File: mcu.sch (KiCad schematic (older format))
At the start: 23 parts, among them U6 LPC55S16JBD64E, Y1 16 MHz, Y2 32.768 kHz

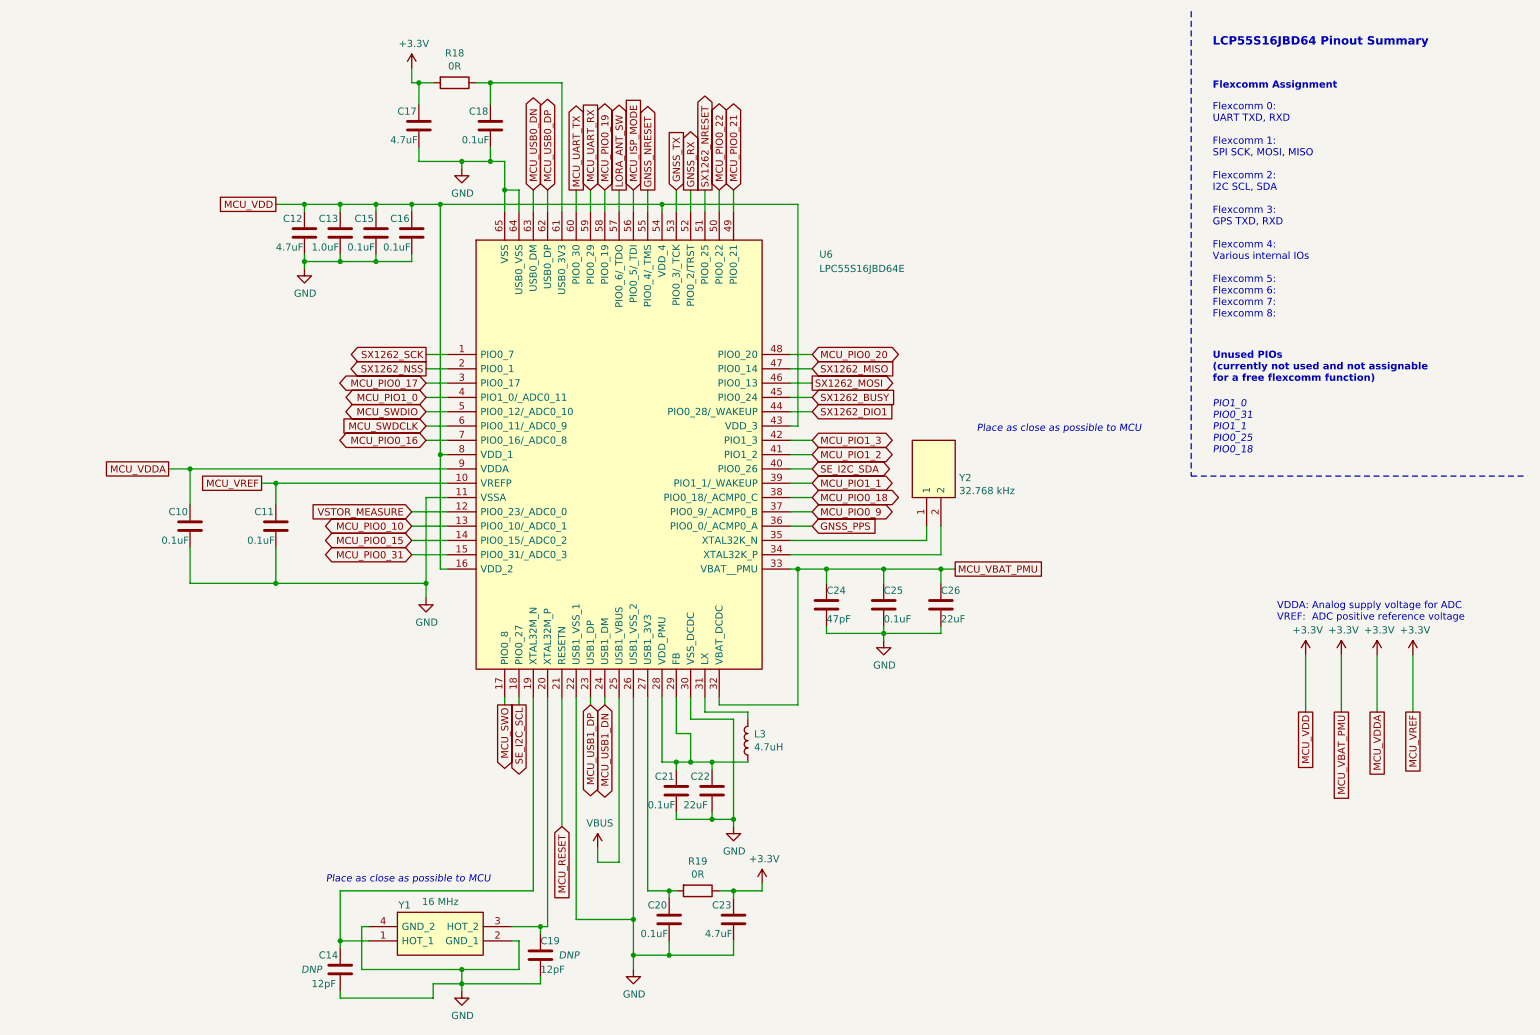
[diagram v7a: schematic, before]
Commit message: Changed pin assignment on mcu and extension header
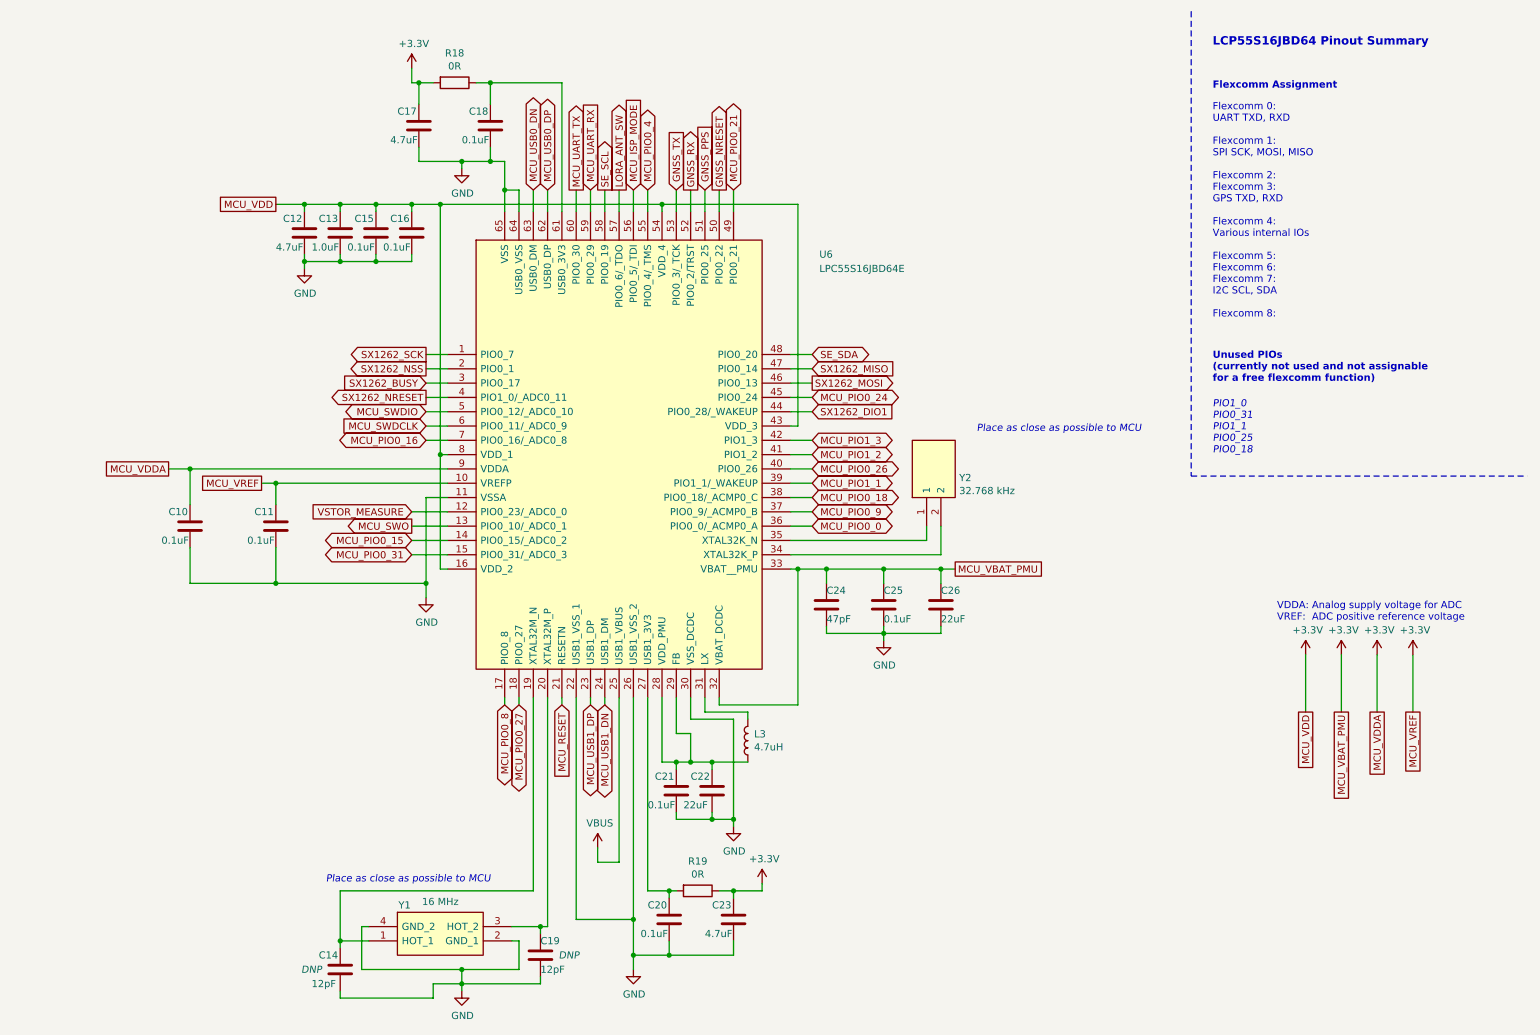
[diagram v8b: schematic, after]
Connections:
- net MCU_PIO0_10 is gone; now on net MCU_SWO: U6.13 (PIO0_10/_ADC0_1)
- net MCU_PIO0_17 is gone; now on net SX1262_BUSY: U6.3 (PIO0_17)
- net MCU_PIO0_22 is gone; now on net GNSS_NRESET: U6.50 (PIO0_22)
- net MCU_PIO1_0 is gone; now on net SX1262_NRESET: U6.4 (PIO1_0/_ADC0_11)
- net GNSS_NRESET: no longer U6.55 (PIO0_4/_TMS)
- net GNSS_PPS: now also U6.51 (PIO0_25); no longer U6.36 (PIO0_0/_ACMP0_A)
- net MCU_SWO: no longer U6.17 (PIO0_8)
- net SX1262_BUSY: no longer U6.45 (PIO0_24)
- net SX1262_NRESET: no longer U6.51 (PIO0_25)
- net MCU_PIO0_19 renamed SE_SCL
- net MCU_PIO0_20 renamed SE_SDA
- net SE_I2C_SCL renamed MCU_PIO0_27
- net SE_I2C_SDA renamed MCU_PIO0_26
- new net MCU_PIO0_0: U6.36 (PIO0_0/_ACMP0_A)
- new net MCU_PIO0_24: U6.45 (PIO0_24)
- new net MCU_PIO0_4: U6.55 (PIO0_4/_TMS)
- new net MCU_PIO0_8: U6.17 (PIO0_8)
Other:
- note added: "Flexcomm 0:\nUART TXD, RXD\n\nFlexcomm 1:\nSPI SCK, MOSI, MISO\n\nFlexcomm 2:\nFlexcomm 3:\nGPS TXD, RXD\n\nFlexcomm 4:\nVarious internal IOs\n\nFlexcomm 5:\nFlexcomm 6:\nFlexcomm 7:\nI2C SCL, SDA\n\nFlexcomm 8:"
- note removed: "Flexcomm 0:\nUART TXD, RXD\n\nFlexcomm 1:\nSPI SCK, MOSI, MISO\n\nFlexcomm 2:\nI2C SCL, SDA\n\nFlexcomm 3:\nGPS TXD, RXD\n\nFlexcomm 4:\nVarious internal IOs\n\nFlexcomm 5:\nFlexcomm 6:\nFlexcomm 7:\nFlexcomm 8:"
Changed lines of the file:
@@
 Wire Wire Line
 	3500 7300 3700 7300
-Text GLabel 4400 6200 3    50   Input ~ 0
+Text GLabel 4400 5350 3    50   Input ~ 0
 MCU_RESET
 Wire Wire Line
-	4400 5300 4400 6200
+	4400 5300 4400 5350
 Text GLabel 4700 5350 3    50   BiDi ~ 0
 MCU_USB1_DN
@@
 Wire Wire Line
 	2400 4500 3450 4500
-Text GLabel 4000 5350 3    50   Output ~ 0
+Text GLabel 3350 4100 0    50   Output ~ 0
 MCU_SWO
 Wire Wire Line
@@
 Text GLabel 4300 1750 1    50   BiDi ~ 0
 MCU_USB0_DP
-Text GLabel 4700 1750 1    50   BiDi ~ 0
-MCU_PIO0_19
-Text GLabel 5500 1750 1    50   BiDi ~ 0
-MCU_PIO0_22
-Text GLabel 5600 1750 1    50   BiDi ~ 0
-MCU_PIO0_21
 Wire Wire Line
 	4200 1750 4200 1900
@@
 Wire Wire Line
 	5600 1750 5600 1900
-Text GLabel 6150 2900 2    50   BiDi ~ 0
-MCU_PIO0_20
 Text GLabel 6150 3500 2    50   BiDi ~ 0
 MCU_PIO1_3
@@
 Text GLabel 6150 3800 2    50   BiDi ~ 0
 MCU_PIO1_1
-Text GLabel 6150 3900 2    50   BiDi ~ 0
-MCU_PIO0_18
 Text GLabel 6150 4000 2    50   BiDi ~ 0
 MCU_PIO0_9
@@
 Text GLabel 6150 3300 2    50   Input ~ 0
 SX1262_DIO1
-Text GLabel 6150 3200 2    50   Input ~ 0
+Text GLabel 3450 3100 0    50   Input ~ 0
 SX1262_BUSY
 Text GLabel 6150 3000 2    50   Input ~ 0
@@
 Text GLabel 6150 3100 2    50   Output ~ 0
 SX1262_MOSI
-Text GLabel 3350 4100 0    50   BiDi ~ 0
-MCU_PIO0_10
 Wire Wire Line
 	6000 3100 6150 3100
 Text GLabel 3450 2900 0    50   Output ~ 0
 SX1262_SCK
-Text GLabel 6150 3700 2    50   BiDi ~ 0
-SE_I2C_SDA
-Text GLabel 4100 5350 3    50   Output ~ 0
-SE_I2C_SCL
+Text GLabel 6150 2900 2    50   BiDi ~ 0
+SE_SDA
+Text GLabel 4700 1750 1    50   Output ~ 0
+SE_SCL
 Text GLabel 5300 1750 1    50   Output ~ 0
 GNSS_RX
@@
 MCU_UART_TX
 Text Notes 8950 2650 0    50   ~ 0
-Flexcomm 0:\nUART TXD, RXD\n\nFlexcomm 1:\nSPI SCK, MOSI, MISO\n\nFlexcomm 2:\nI2C SCL, SDA\n\nFlexcomm 3:\nGPS TXD, RXD\n\nFlexcomm 4:\nVarious internal IOs\n\nFlexcomm 5:\nFlexcomm 6:\nFlexcomm 7:\nFlexcomm 8:
-Text GLabel 5400 1750 1    50   Output ~ 0
+Flexcomm 0:\nUART TXD, RXD\n\nFlexcomm 1:\nSPI SCK, MOSI, MISO\n\nFlexcomm 2:\nFlexcomm 3:\nGPS TXD, RXD\n\nFlexcomm 4:\nVarious internal IOs\n\nFlexcomm 5:\nFlexcomm 6:\nFlexcomm 7:\nI2C SCL, SDA\n\nFlexcomm 8:
+Text GLabel 3450 3200 0    50   Output ~ 0
 SX1262_NRESET
 Text Notes 8950 3600 0    50   Italic 0
@@
 Wire Wire Line
 	6150 3300 6000 3300
-Wire Wire Line
-	6150 3200 6000 3200
 Text GLabel 3450 3000 0    50   Output ~ 0
 SX1262_NSS
-Text GLabel 4800 1750 1    50   Output ~ 0
-LORA_ANT_SW
 Wire Wire Line
 	5400 1750 5400 1900
 Wire Wire Line
 	4800 1750 4800 1900
-Text GLabel 5000 1750 1    50   Output ~ 0
+Text GLabel 5500 1750 1    50   Output ~ 0
 GNSS_NRESET
-Text GLabel 6150 4100 2    50   Input ~ 0
+Text GLabel 5400 1750 1    50   Input ~ 0
 GNSS_PPS
 Wire Wire Line
@@
 Wire Wire Line
 	3450 3200 3600 3200
-Text GLabel 3450 3200 0    50   BiDi ~ 0
-MCU_PIO1_0
 Wire Wire Line
 	3450 3500 3600 3500
@@
 Wire Wire Line
 	4300 5300 4300 6900
-Text Notes 7300 3450 0    50   Italic 0
-Place as close as possible to MCU
 Text Notes 2750 6600 0    50   Italic 0
 Place as close as possible to MCU
@@
 Wire Wire Line
 	5450 6150 5600 6150
-Text GLabel 3450 3100 0    50   BiDi ~ 0
-MCU_PIO0_17
 Wire Wire Line
 	9600 5000 9600 5400
@@
 Wire Wire Line
 	7050 4400 7150 4400
+Text Notes 7300 3450 0    50   Italic 0
+Place as close as possible to MCU
+Text GLabel 4800 1750 1    50   Output ~ 0
+LORA_ANT_SW
+Text GLabel 5000 1750 1    50   BiDi ~ 0
+MCU_PIO0_4
+Text GLabel 6150 3200 2    50   BiDi ~ 0
+MCU_PIO0_24
+Wire Wire Line
+	6000 3200 6150 3200
+Text GLabel 6150 4100 2    50   BiDi ~ 0
+MCU_PIO0_0
+Text GLabel 6150 3900 2    50   BiDi ~ 0
+MCU_PIO0_18
+Text GLabel 6150 3700 2    50   BiDi ~ 0
+MCU_PIO0_26
+Text GLabel 4100 5350 3    50   BiDi ~ 0
+MCU_PIO0_27
+Text GLabel 4000 5350 3    50   BiDi ~ 0
+MCU_PIO0_8
+Text GLabel 5600 1750 1    50   BiDi ~ 0
+MCU_PIO0_21
 $EndSCHEMATC
